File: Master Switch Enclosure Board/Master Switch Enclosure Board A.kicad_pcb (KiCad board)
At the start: 2 copper layers, 40 parts, among them IC1 LM5155DSSR, J1 Harness In A, J2 Harness In B, J3 Harness Out, J4 Screw_Terminal_01x04, J5 Screw_Terminal_01x04, J6 18-pin MicroFit, J7 4-pin MicroFit, Q1 CSD18537NQ5A

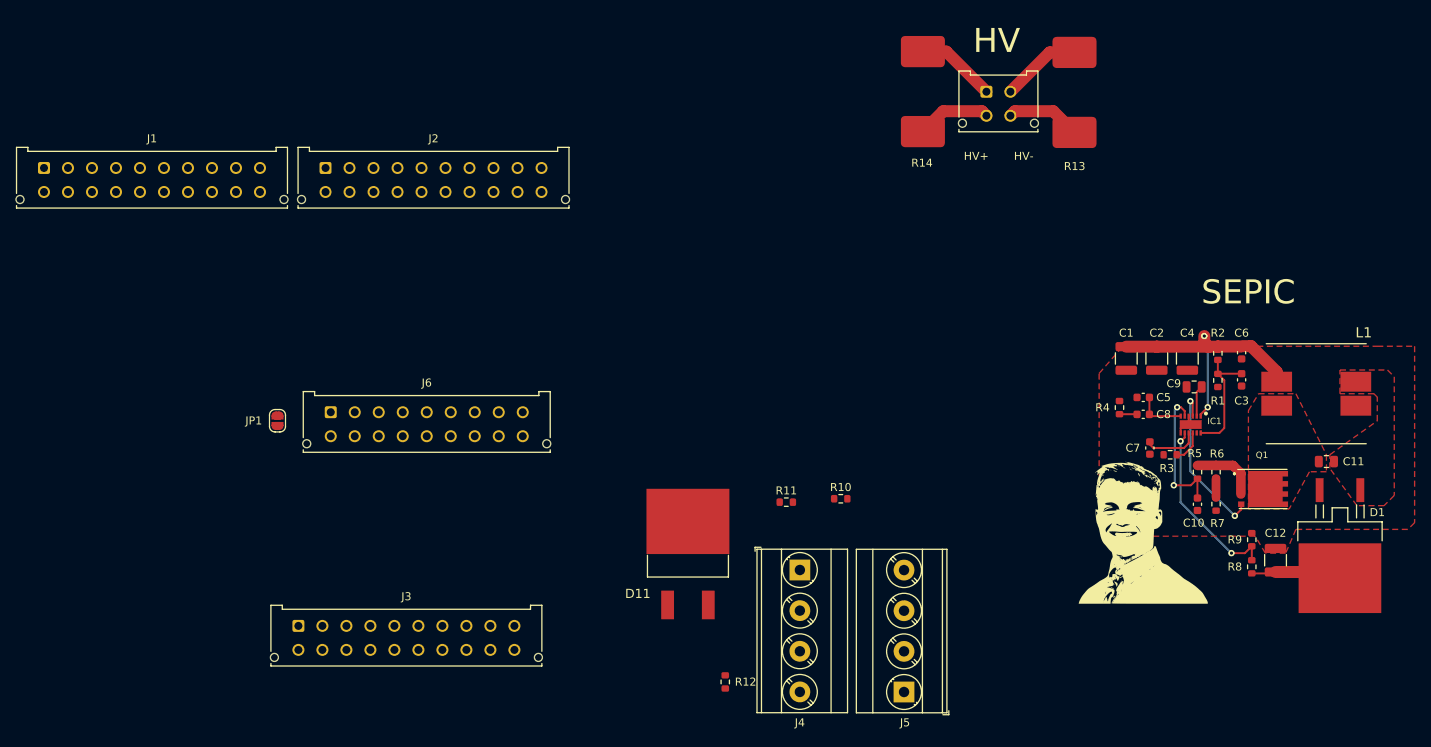
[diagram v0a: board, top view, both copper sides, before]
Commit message: remove second board
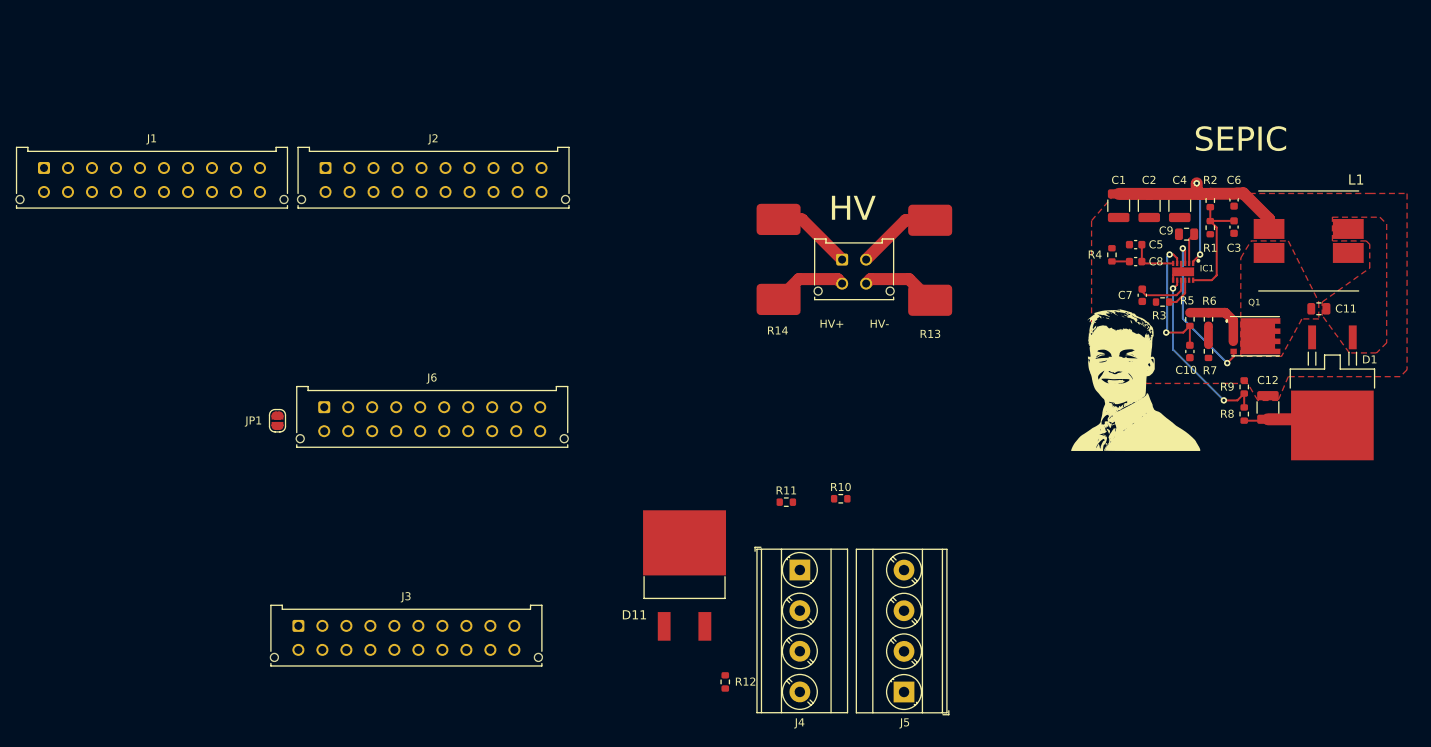
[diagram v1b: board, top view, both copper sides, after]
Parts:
- J6: value 18-pin MicroFit -> 20-pin MicroFit; footprint Connector_Molex:Molex_Micro-Fit_3.0_43045-1812_2x09_P3.00mm_Vertical -> Connector_Molex:Molex_Micro-Fit_3.0_43045-2012_2x10_P3.00mm_Vertical
- moved J7 27.7 mm to (143.9, 75.7)
- moved R14 27.7 mm to (133.0, 75.7)
- moved R13 27.7 mm to (151.9, 75.8)
- moved C1 19.1 mm to (178.5, 68.9)
- moved C10 19.1 mm to (187.4, 87.2)
- moved C11 19.1 mm to (203.5, 81.8)
- moved C4 19.1 mm to (186.1, 68.9)
- moved C6 19.1 mm to (192.9, 68.2)
- moved C7 19.1 mm to (181.4, 80.1)
- moved IC1 19.1 mm to (186.6, 77.2)
- moved Q1 19.1 mm to (195.3, 85.3)
- moved R1 19.1 mm to (189.9, 71.7)
- moved R2 19.1 mm to (189.9, 68.3)
- moved R8 19.1 mm to (194.2, 95.0)
- moved R9 19.1 mm to (194.2, 91.6)
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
